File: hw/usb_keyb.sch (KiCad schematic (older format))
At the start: 9 parts

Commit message: Начальны вариант схемы
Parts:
- added C? (x2): 22pF, symbol C
- added C?: 100uF, symbol CP
- added C? (x8): 100n, symbol C
- added J?: Micro_SD_Card_Det, symbol Micro_SD_Card_Det
- added J?: MX_ROW, symbol Conn_01x12
- added J?: MX_COL, symbol Conn_01x12
- added J?: POWER, symbol Conn_01x04
- added R? (x36): 10k, symbol R
- added SW?: RESET, symbol SW_Push
- added U? (x4): 74ALVC164245, symbol 74ALVC164245
- added Y?: 8MHz, symbol Crystal
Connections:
- net labels added: BOOT0, BOOT1, C0, C1, C10, C11, C2, C3, C4, C5, C6, C7, C8, C9, CD, CK, CMD, D0, D1, D2, D3, DR0, DR1, DR2, DR3, DR4, DR5, DR6, DR7, I0, I1, I10, I11, I2, I3, I4, I5, I6, I7, I8, I9, INT0, INT1, INT2, INT3, O0, O1, O10, O11, O2, O3, O4, O5, O6, O7, O8, O9, OSC_IN, OSC_OUT, R0, R1, R10, R11, R2, R3, R4, R5, R6, R7, R8, R9, RES, SCL, SDA, SPI_MISO, SPI_MOSI, SPI_NSS, SPI_SCK, SWCLK, SWDIO, UART3_RX, UART3_TX, VB, VC1, VC2, VR+
- wire segments 28 -> 112

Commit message: Схема обновлена до максимального варианта.
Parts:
- added C?: 4,7uF, symbol CP
- added C? (x3): 100n, symbol C
- added J?: USB_2, symbol USB_A
- added J?: ID, symbol TEST_1P
- added J?: ZX BUS, symbol Conn_02x28_Odd_Even
- added J?: PROG, symbol Conn_01x05
- added J?: SPI, symbol Conn_01x06
- added J?: I2C, symbol Conn_01x04
- added J?: UART, symbol Conn_01x04
- added R? (x3): 10k, symbol R
- added R?: 0, symbol R
- added R? (x2): 22, symbol R
- added U?: STMPS2141STR, symbol STMPS2141STR
- added U?: 74ALVC164245, symbol 74ALVC164245
- J?: value USB_A -> USB_1
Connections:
- net labels added: +5, A0, A1, A2, A3, A4, A5, A6, A7, CLK, FS_D+, FS_D-, FS_ID, FS_PWR, FS_VBUS, HS_D+, HS_D-, HS_ID, HS_PWR, HS_VBUS, INTn, M1n, MC10, MC11, MC8, MC9, MR10, MR11, MR8, MR9, NMIn, PA4, PA8, SPI_CS, ZA0, ZA1, ZA10, ZA11, ZA12, ZA13, ZA14, ZA15, ZA2, ZA3, ZA4, ZA5, ZA6, ZA7, ZA8, ZA9, ZBUSACKn, ZBUSRQn, ZD0, ZD1, ZD2, ZD3, ZD4, ZD5, ZD6, ZD7, ZHALTn, ZINTn, ZIORQn, ZM1n, ZMREQn, ZNMIn, ZRDn, ZRESn, ZRFSHn, ZWAITn, ZWRn
- net labels removed: BOOT1, PA10, PA11, PA12, PA9, PC0, SPI_NSS
- wire segments 112 -> 216
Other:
- moved on the sheet: C?, J?, R?, U?, U?A

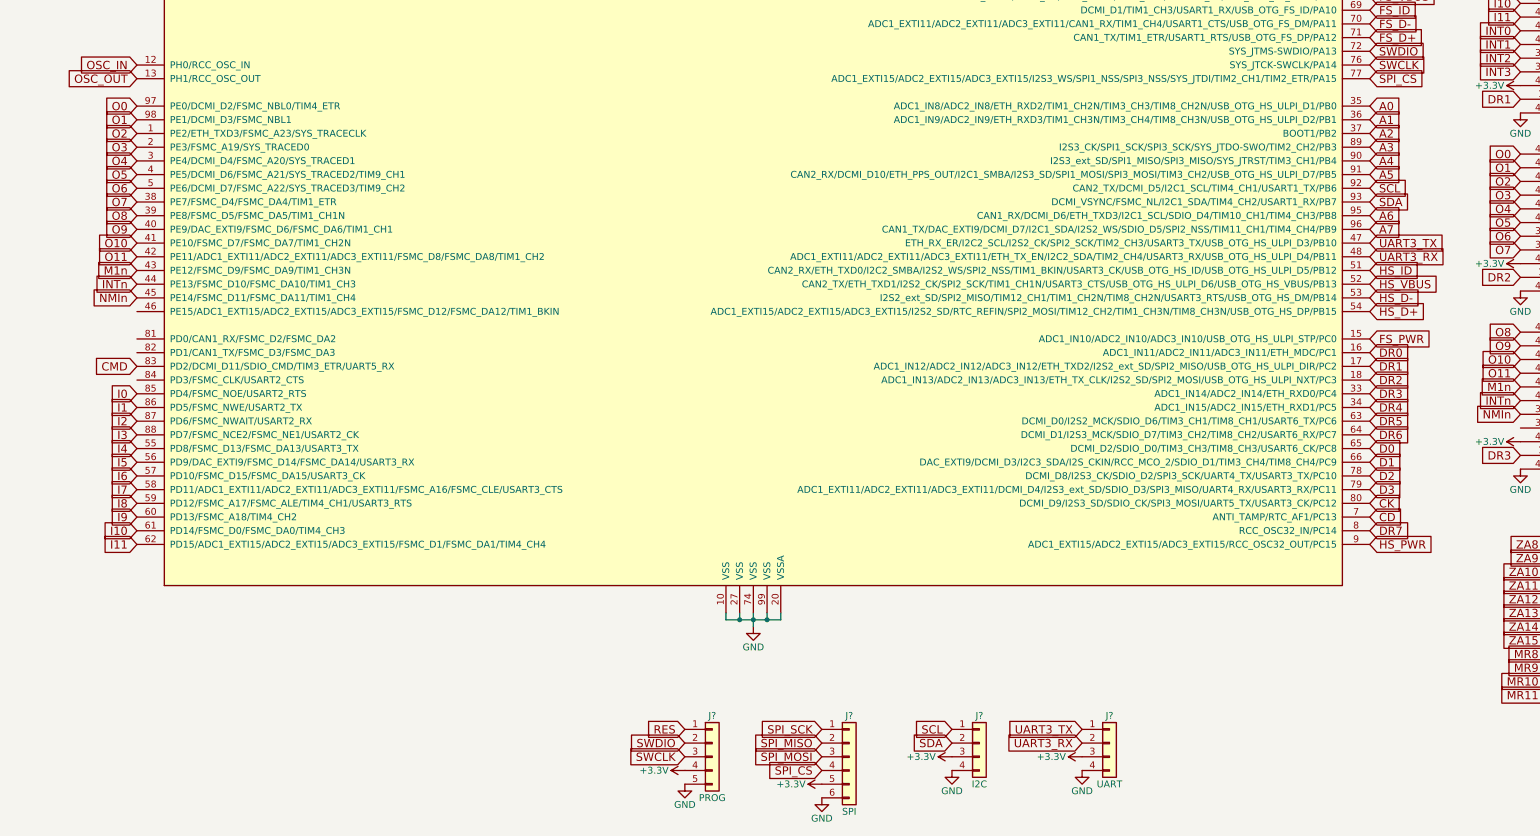
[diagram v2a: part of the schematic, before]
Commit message: Оптимизировано расположение выводов и добавлены контрольные линии RS232
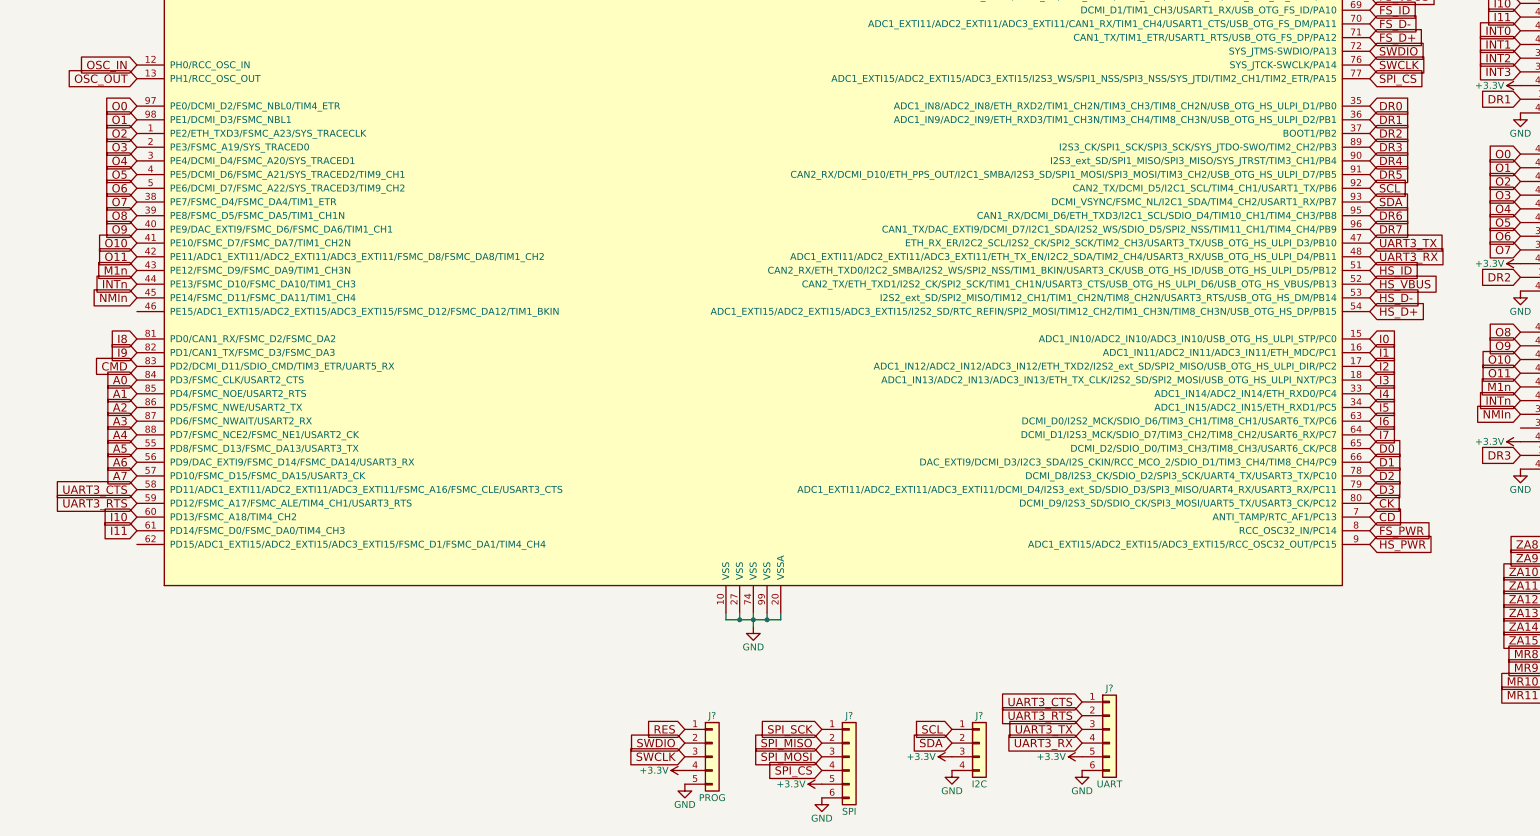
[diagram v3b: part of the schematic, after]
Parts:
- removed J?: UART, symbol Conn_01x04
- added J?: UART, symbol Conn_01x06
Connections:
- net labels added: UART3_CTS, UART3_RTS
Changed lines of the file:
@@
 	1    0    0    -1
 $EndComp
-Text GLabel 10750 7050 2    60   Input ~ 0
+Text GLabel 10750 8450 2    60   Input ~ 0
 FS_PWR
 Text GLabel 10750 4550 2    60   Input ~ 0
@@
 Text GLabel 1750 7250 0    60   Input ~ 0
 CMD
-Text GLabel 1750 7450 0    60   Input ~ 0
+Text GLabel 10750 7050 2    60   Input ~ 0
 I0
-Text GLabel 1750 7550 0    60   Input ~ 0
+Text GLabel 10750 7150 2    60   Input ~ 0
 I1
-Text GLabel 1750 7650 0    60   Input ~ 0
+Text GLabel 10750 7250 2    60   Input ~ 0
 I2
-Text GLabel 1750 7750 0    60   Input ~ 0
+Text GLabel 10750 7350 2    60   Input ~ 0
 I3
-Text GLabel 1750 7850 0    60   Input ~ 0
+Text GLabel 10750 7450 2    60   Input ~ 0
 I4
-Text GLabel 1750 7950 0    60   Input ~ 0
+Text GLabel 10750 7550 2    60   Input ~ 0
 I5
-Text GLabel 1750 8050 0    60   Input ~ 0
+Text GLabel 10750 7650 2    60   Input ~ 0
 I6
-Text GLabel 1750 8150 0    60   Input ~ 0
+Text GLabel 10750 7750 2    60   Input ~ 0
 I7
-Text GLabel 1750 8250 0    60   Input ~ 0
+Text GLabel 1750 7050 0    60   Input ~ 0
 I8
+Text GLabel 1750 7150 0    60   Input ~ 0
+I9
 Text GLabel 1750 8350 0    60   Input ~ 0
-I9
+I10
 Text GLabel 1750 8450 0    60   Input ~ 0
-I10
-Text GLabel 1750 8550 0    60   Input ~ 0
 I11
 Text GLabel 1750 5350 0    60   Input ~ 0
@@
 Text GLabel 11850 7900 0    60   Input ~ 0
 DR3
-Text GLabel 10750 7150 2    60   Input ~ 0
+Text GLabel 10750 5350 2    60   Input ~ 0
 DR0
-Text GLabel 10750 7250 2    60   Input ~ 0
+Text GLabel 10750 5450 2    60   Input ~ 0
 DR1
-Text GLabel 10750 7350 2    60   Input ~ 0
+Text GLabel 10750 5550 2    60   Input ~ 0
 DR2
-Text GLabel 10750 7450 2    60   Input ~ 0
+Text GLabel 10750 5650 2    60   Input ~ 0
 DR3
-Text GLabel 10750 7550 2    60   Input ~ 0
+Text GLabel 10750 5750 2    60   Input ~ 0
 DR4
-Text GLabel 10750 7650 2    60   Input ~ 0
+Text GLabel 10750 5850 2    60   Input ~ 0
 DR5
-Text GLabel 10750 7750 2    60   Input ~ 0
+Text GLabel 10750 6150 2    60   Input ~ 0
 DR6
-Text GLabel 10750 8450 2    60   Input ~ 0
+Text GLabel 10750 6250 2    60   Input ~ 0
 DR7
 Text GLabel 10750 5950 2    60   Input ~ 0
@@
 $EndComp
 $Comp
-L Conn_01x04 J?
-U 1 1 5AB61FE4
-P 8850 10000
-F 0 "J?" H 8850 10200 50  0000 C CNN
-F 1 "UART" H 8850 9700 50  0000 C CNN
-F 2 "" H 8850 10000 50  0001 C CNN
-F 3 "" H 8850 10000 50  0001 C CNN
-	1    8850 10000
-	1    0    0    -1
-$EndComp
-$Comp
 L +3.3V #PWR?
 U 1 1 5AB62226
@@
 Text GLabel 13250 5100 2    60   Input ~ 0
 ZMREQn
-Text GLabel 10750 5350 2    60   Input ~ 0
+Text GLabel 1750 7350 0    60   Input ~ 0
 A0
-Text GLabel 10750 5450 2    60   Input ~ 0
+Text GLabel 1750 7450 0    60   Input ~ 0
 A1
-Text GLabel 10750 5550 2    60   Input ~ 0
+Text GLabel 1750 7550 0    60   Input ~ 0
 A2
-Text GLabel 10750 5650 2    60   Input ~ 0
+Text GLabel 1750 7650 0    60   Input ~ 0
 A3
-Text GLabel 10750 5750 2    60   Input ~ 0
+Text GLabel 1750 7750 0    60   Input ~ 0
 A4
-Text GLabel 10750 5850 2    60   Input ~ 0
+Text GLabel 1750 7850 0    60   Input ~ 0
 A5
-Text GLabel 10750 6150 2    60   Input ~ 0
+Text GLabel 1750 7950 0    60   Input ~ 0
 A6
-Text GLabel 10750 6250 2    60   Input ~ 0
+Text GLabel 1750 8050 0    60   Input ~ 0
 A7
+Text GLabel 1750 8250 0    60   Input ~ 0
+UART3_RTS
+Text GLabel 1750 8150 0    60   Input ~ 0
+UART3_CTS
+Text GLabel 8650 9800 0    60   Input ~ 0
+UART3_RTS
+Text GLabel 8650 9700 0    60   Input ~ 0
+UART3_CTS
+$Comp
+L Conn_01x06 J?
+U 1 1 5AB754D7
+P 8850 9900
+F 0 "J?" H 8850 10200 50  0000 C CNN
+F 1 "UART" H 8850 9500 50  0000 C CNN
+F 2 "" H 8850 9900 50  0001 C CNN
+F 3 "" H 8850 9900 50  0001 C CNN
+	1    8850 9900
+	1    0    0    -1
+$EndComp
 $EndSCHEMATC

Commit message: Добавлено питание и обозначены компоненты
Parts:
- added C1, C2: 100u, Capacitors_SMD:CP_Elec_5x5.7, symbol CP
- added C19, C20, C21, C22, C23, C24, C25, C26, C27, C28, C29, C30: 100n, Capacitors_SMD:C_0805, symbol C
- added JP1, JP2: 5Vin, Pin_Headers:Pin_Header_Straight_1x02_Pitch2.54mm, symbol Jumper_NC_Small
- added JP3: 3Vin, Pin_Headers:Pin_Header_Straight_1x02_Pitch2.54mm, symbol Jumper_NC_Small
- added L1: 2.2µH, Inductors_SMD:L_Vishay_IHLP-1616, symbol L
- added R1: 10k, Resistors_SMD:R_0805, symbol R
- added U1: LM3671MF, TO_SOT_Packages_SMD:SOT-23-5, symbol LM3671MF
- C10, C11, C12, C14, C15, C16, C3, C4, C5, C6, C7, C8, C9: renamed from C?; footprint (none) -> Capacitors_SMD:C_0805
- C13: renamed from C?; footprint (none) -> Capacitors_SMD:CP_Elec_5x5.7
- C17, C18: renamed from C?; footprint (none) -> Capacitors_Tantalum_SMD:CP_Tantalum_Case-A_EIA-3216-18_Hand
- J10, J8: renamed from J?; footprint (none) -> Socket_Strips:Socket_Strip_Straight_1x06_Pitch2.54mm
- J12, J13: renamed from J?; footprint (none) -> Socket_Strips:Socket_Strip_Straight_1x01_Pitch2.54mm
- J2: renamed from J?; value Micro_SD_Card_Det -> MicroSD
- J3, J4: renamed from J?; footprint (none) -> Connectors:USB_A
- J5, J6: renamed from J?; footprint (none) -> Socket_Strips:Socket_Strip_Straight_1x11_Pitch2.54mm
- J7: renamed from J?; footprint (none) -> Socket_Strips:Socket_Strip_Straight_1x04_Pitch2.54mm
- J9: renamed from J?; footprint (none) -> Socket_Strips:Socket_Strip_Straight_1x05_Pitch2.00mm
- R10, R11, R12, R13, R14, R15, R16, R17, R18, R19, R2, R20, R21, R22, R23, R24, R25, R26, R27, R28, R29, R3, R30, R31, R32, R33, R34, R35, R36, R37, R38, R39, R4, R40, R41, R42, R43, R44, R45, R46, R47, R5, R6, R7, R8, R9: renamed from R?; footprint (none) -> Resistors_SMD:R_0805
- SW1: renamed from SW?; footprint (none) -> Buttons_Switches_THT:SW_Tactile_SPST_Angled_PTS645Vx83-2LFS
- U2: renamed from U?; footprint LQFP100 -> Housings_QFP:LQFP-100_14x14mm_Pitch0.5mm
- U3, U4: renamed from U?; footprint (none) -> TO_SOT_Packages_SMD:SOT-23-5
- U5, U6, U7: renamed from U?; footprint (none) -> Housings_SSOP:SSOP-48_7.5x15.9mm_Pitch0.635mm
- Y1: renamed from Y?; footprint (none) -> Crystals:Crystal_HC49-4H_Vertical
- gave numbers to parts that had none: 2
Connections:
- wire segments 216 -> 183
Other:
- moved on the sheet: C10, C11, C12, C16, C3, C4, C5, C6, C7, C8, C9, J1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

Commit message: Предварительная компоновка элементов на плате
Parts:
- removed J2: MicroSD, symbol Micro_SD_Card_Det
- added J2: Micro_SD_Card, Projects:Conn_uSDcard, symbol Micro_SD_Card
- J1: footprint (none) -> Connectors_Phoenix:PhoenixContact_GMSTBA-G_04x7.50mm_Angled
- J5, J6: footprint Socket_Strips:Socket_Strip_Straight_1x11_Pitch2.54mm -> Socket_Strips:Socket_Strip_Straight_1x12_Pitch2.54mm
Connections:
- wire segments 183 -> 182
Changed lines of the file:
@@
 EESchema Schematic File Version 2
+LIBS:mem
 LIBS:power
 LIBS:device
@@
 LIBS:contrib
 LIBS:valves
-LIBS:mem
 LIBS:usb_keyb-cache
 EELAYER 25 0
@@
 	1    0    0    -1
 $EndComp
-$Comp
-L Micro_SD_Card_Det J2
-U 1 1 5AB15F8B
-P 9300 2000
-F 0 "J2" H 8650 2700 50  0000 C CNN
-F 1 "MicroSD" H 9950 2700 50  0000 R CNN
-F 2 "" H 11350 2700 50  0001 C CNN
-F 3 "" H 9300 2100 50  0001 C CNN
-	1    9300 2000
-	1    0    0    -1
-$EndComp
 Text GLabel 8400 1600 0    60   Input ~ 0
 D2
@@
 L GND #PWR013
 U 1 1 5AB17E87
-P 7900 2600
-F 0 "#PWR013" H 7900 2350 50  0001 C CNN
-F 1 "GND" H 7900 2450 50  0000 C CNN
-F 2 "" H 7900 2600 50  0001 C CNN
-F 3 "" H 7900 2600 50  0001 C CNN
-	1    7900 2600
+P 7900 2250
+F 0 "#PWR013" H 7900 2000 50  0001 C CNN
+F 1 "GND" H 8025 2200 50  0000 C CNN
+F 2 "" H 7900 2250 50  0001 C CNN
+F 3 "" H 7900 2250 50  0001 C CNN
+	1    7900 2250
 	1    0    0    -1
 $EndComp
@@
 F 0 "J5" H 12250 9650 50  0000 C CNN
 F 1 "MX_ROW" H 12250 8350 50  0000 C CNN
-F 2 "Socket_Strips:Socket_Strip_Straight_1x11_Pitch2.54mm" H 12250 9050 50  0001 C CNN
+F 2 "Socket_Strips:Socket_Strip_Straight_1x12_Pitch2.54mm" H 12250 9050 50  0001 C CNN
 F 3 "" H 12250 9050 50  0001 C CNN
 	1    12250 9050
@@
 F 0 "J6" H 13250 9650 50  0000 C CNN
 F 1 "MX_COL" H 13250 8350 50  0000 C CNN
-F 2 "Socket_Strips:Socket_Strip_Straight_1x11_Pitch2.54mm" H 13250 9050 50  0001 C CNN
+F 2 "Socket_Strips:Socket_Strip_Straight_1x12_Pitch2.54mm" H 13250 9050 50  0001 C CNN
 F 3 "" H 13250 9050 50  0001 C CNN
 	1    13250 9050
@@
 F 0 "J1" H 1450 10150 50  0000 C CNN
 F 1 "POWER" H 1450 9650 50  0000 C CNN
-F 2 "" H 1450 9950 50  0001 C CNN
+F 2 "Connectors_Phoenix:PhoenixContact_GMSTBA-G_04x7.50mm_Angled" H 1450 9950 50  0001 C CNN
 F 3 "" H 1450 9950 50  0001 C CNN
 	1    1450 9950
@@
 Connection ~ 7900 1800
 Wire Wire Line
-	7900 2150 7900 2600
-Wire Wire Line
-	7650 2150 7650 2400
-Wire Wire Line
-	7650 2400 8400 2400
-Wire Wire Line
-	8400 2500 7900 2500
-Connection ~ 7900 2500
+	7900 2150 7900 2250
 Wire Wire Line
 	8400 2100 8150 2100
@@
 	1    0    0    -1
 $EndComp
+Wire Wire Line
+	7600 2400 8400 2400
+Text GLabel 7600 2400 0    60   Input ~ 0
+CD
+Connection ~ 7650 2400
+$Comp
+L Micro_SD_Card J2
+U 1 1 5ABCF5FB
+P 9300 2000
+F 0 "J2" H 8650 2550 50  0000 C CNN
+F 1 "Micro_SD_Card" H 9900 1450 50  0000 C CNN
+F 2 "Projects:Conn_uSDcard" H 9500 2350 50  0000 C CNN
+F 3 "" H 9300 2000 50  0000 C CNN
+	1    9300 2000
+	1    0    0    -1
+$EndComp
+Wire Wire Line
+	7650 2400 7650 2150
 $EndSCHEMATC
